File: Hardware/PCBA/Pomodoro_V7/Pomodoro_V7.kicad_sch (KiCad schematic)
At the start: 0 parts

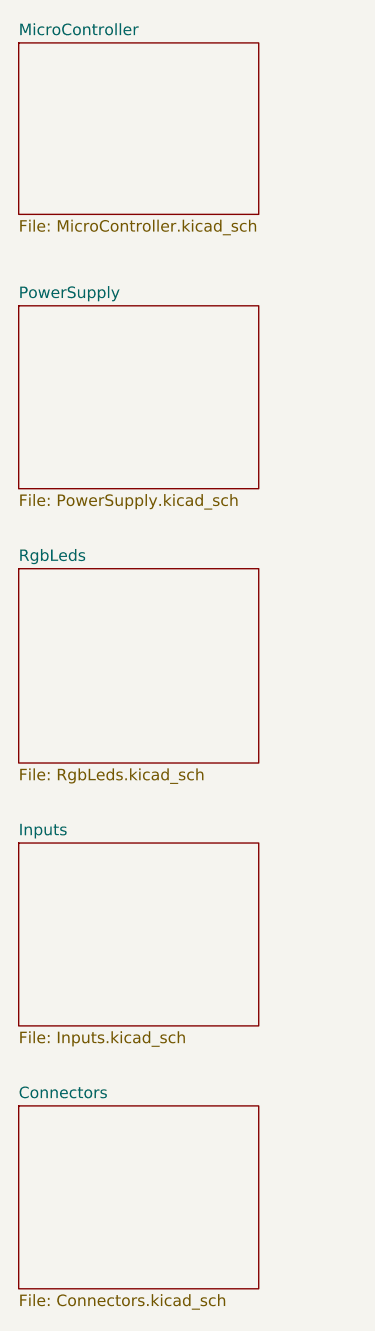
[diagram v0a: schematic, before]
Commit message: FW can now be flashed to an ESP32-S2 Target; Completed the Schematic
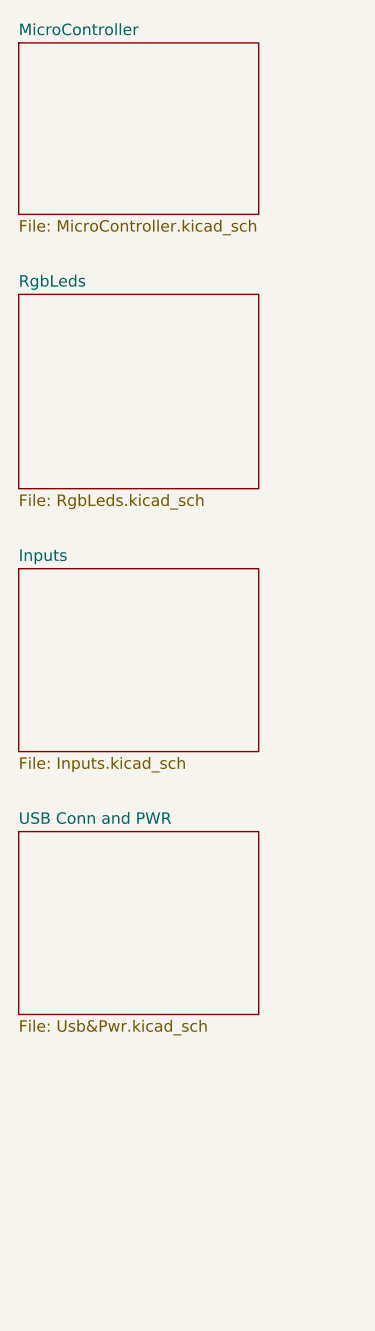
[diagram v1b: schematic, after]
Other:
- sheet Connectors renamed USB Conn and PWR 
- removed sheet PowerSupply
- sheet USB Conn and PWR : file Connectors.kicad_sch -> Usb&Pwr.kicad_sch
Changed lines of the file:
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@@
 	(paper "A4")
 	(sheet
-		(at 33.02 146.05)
+		(at 33.02 115.57)
 		(size 26.67 20.32)
 		(fields_autoplaced yes)
@@
 			(color 0 0 0 0.0000)
 		)
-		(property "Sheetname" "Connectors"
-			(at 33.02 145.3384 0)
+		(property "Sheetname" "USB Conn and PWR "
+			(at 33.02 114.8584 0)
 			(effects
 				(font
@@
 			)
 		)
-		(property "Sheetfile" "Connectors.kicad_sch"
-			(at 33.02 166.9546 0)
+		(property "Sheetfile" "Usb&Pwr.kicad_sch"
+			(at 33.02 136.4746 0)
 			(effects
 				(font
@@
 	)
 	(sheet
-		(at 33.02 57.15)
-		(size 26.67 20.32)
-		(fields_autoplaced yes)
-		(stroke
-			(width 0.1524)
-			(type solid)
-		)
-		(fill
-			(color 0 0 0 0.0000)
-		)
-		(property "Sheetname" "PowerSupply"
-			(at 33.02 56.4384 0)
-			(effects
-				(font
-					(size 1.27 1.27)
-				)
-				(justify left bottom)
-			)
-		)
-		(property "Sheetfile" "PowerSupply.kicad_sch"
-			(at 33.02 78.0546 0)
-			(effects
-				(font
-					(size 1.27 1.27)
-				)
-				(justify left top)
-			)
-		)
-		(instances
-			(project "Pomodoro_V7"
-				(path "/7b50fc13-bee1-48b7-8eab-d6ef36855383"
-					(page "3")
-				)
-			)
-		)
-	)
-	(sheet
-		(at 33.02 116.84)
+		(at 33.02 86.36)
 		(size 26.67 20.32)
 		(fields_autoplaced yes)
@@
 		)
 		(property "Sheetname" "Inputs"
-			(at 33.02 116.1284 0)
+			(at 33.02 85.6484 0)
 			(effects
 				(font
@@
 		)
 		(property "Sheetfile" "Inputs.kicad_sch"
-			(at 33.02 137.7446 0)
+			(at 33.02 107.2646 0)
 			(effects
 				(font
@@
 	)
 	(sheet
-		(at 33.02 86.36)
+		(at 33.02 55.88)
 		(size 26.67 21.59)
 		(fields_autoplaced yes)
@@
 		)
 		(property "Sheetname" "RgbLeds"
-			(at 33.02 85.6484 0)
+			(at 33.02 55.1684 0)
 			(effects
 				(font
@@
 		)
 		(property "Sheetfile" "RgbLeds.kicad_sch"
-			(at 33.02 108.5346 0)
+			(at 33.02 78.0546 0)
 			(effects
 				(font
